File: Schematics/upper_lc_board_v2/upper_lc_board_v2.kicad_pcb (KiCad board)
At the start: 4 copper layers, 69.5 x 60 mm, 115 parts, among them J1 USB_C_Female_USB2_Small, J2 Stack Male Edge Connector, J3 SOL_CONN, J4 SOL_CONN, J5 HALL-1, J7 PT1, J8 PT1, Q2 AO3400A, Q3 AO3400A, Q4 2N7002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

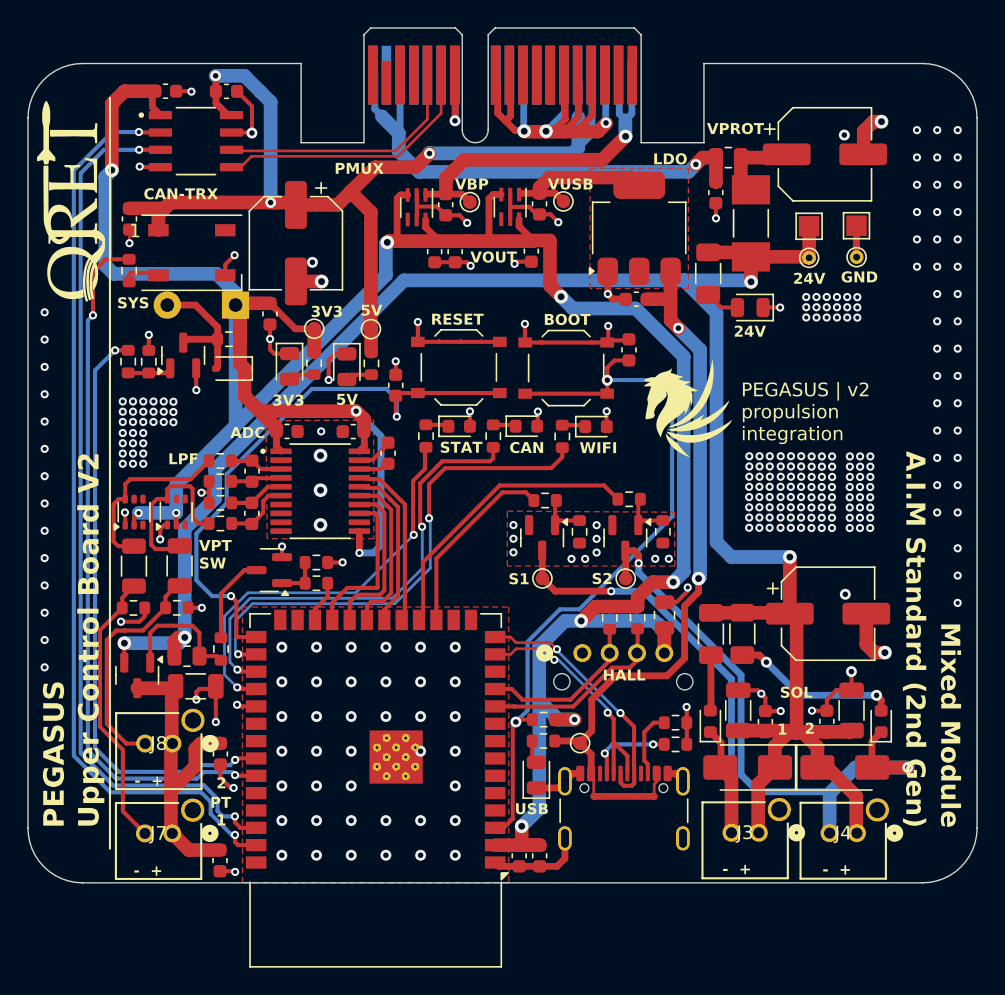
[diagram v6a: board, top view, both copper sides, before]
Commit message: tune diff pairs, increase track width on 5V rail
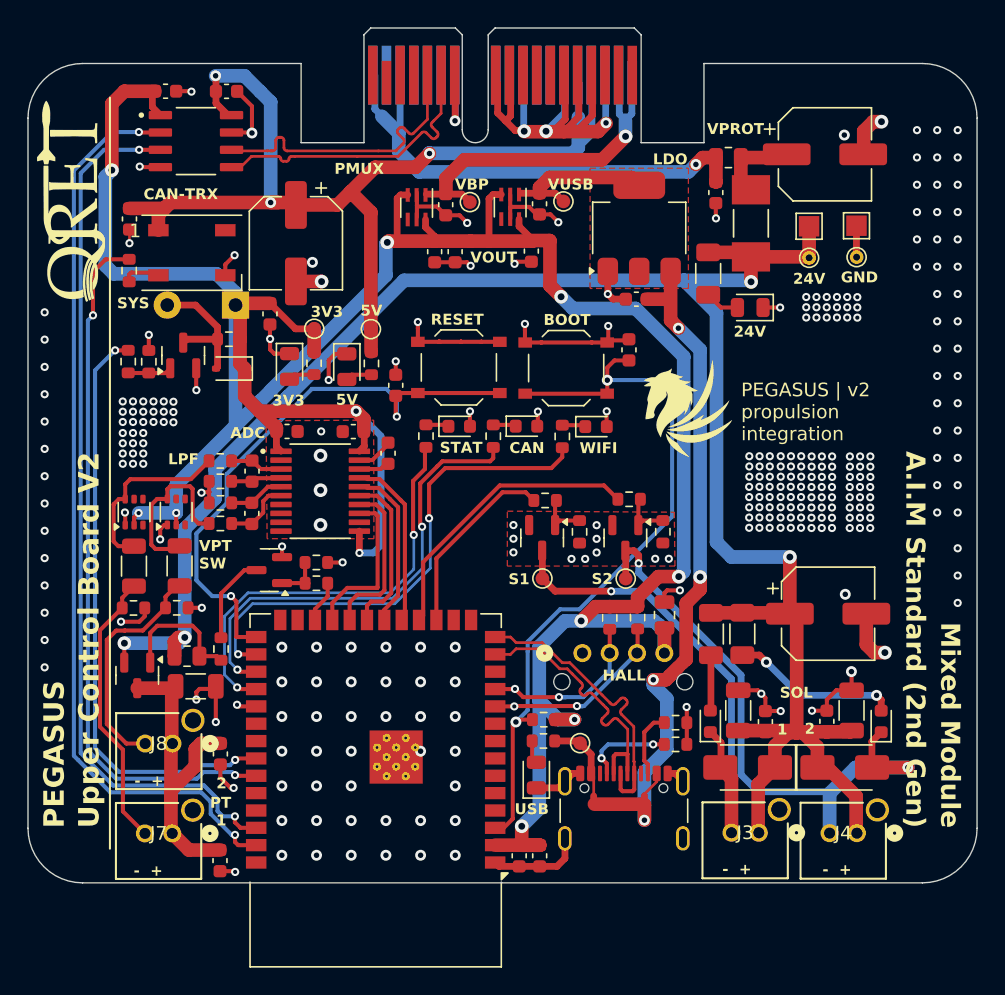
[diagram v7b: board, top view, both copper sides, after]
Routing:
- net 5V_USB: track 55.1 -> 60.3 mm, vias 2 -> 4
- net /ESP32-S3 Breakout Circuitry/USB_N: track 18.0 -> 21.4 mm, vias 2 -> 0
- net CAN_P: track 18.6 -> 21.7 mm
- net /ESP32-S3 Breakout Circuitry/USB_P: track 18.9 -> 21.7 mm, vias 2 -> 0
- net CAN_N: track 19.8 -> 21.7 mm
- net /ESP32-S3 Breakout Circuitry/GPIO_37: track 30.2 -> 31.7 mm
- net HALL_SCL: track 12.2 -> 13.0 mm, vias 0 -> 2
- net HALL_SDA: track 14.1 -> 14.2 mm, vias 0 -> 2

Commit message: refactor with new conns
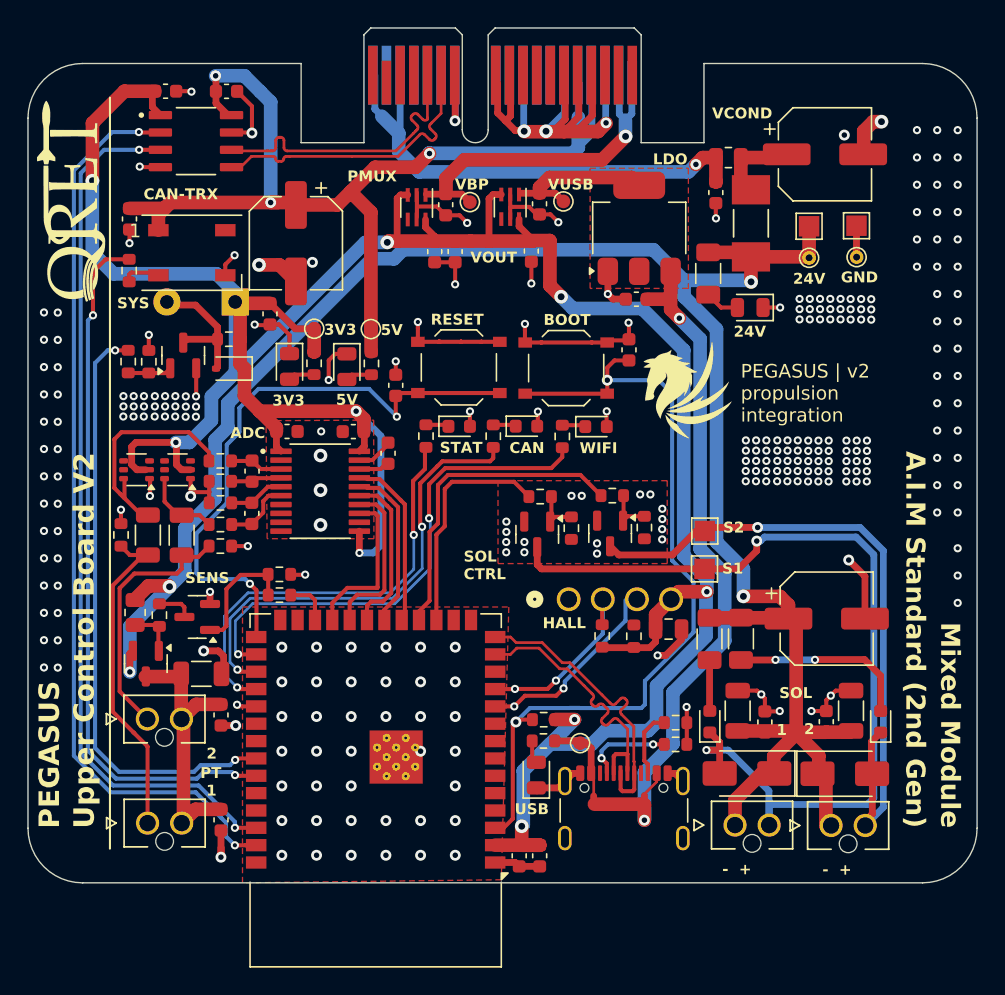
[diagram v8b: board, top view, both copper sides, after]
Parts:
- removed J8: PT1, ul_B02B-PASK-1:CONN_B02B-PASK-1_JST
- removed Q3: AO3400A, Package_TO_SOT_SMD:SOT-23
- removed R32, R35: 1k, Resistor_SMD:R_1206_3216Metric
- removed R34: 60, Resistor_SMD:R_0603_1608Metric
- removed R36: 200, Resistor_SMD:R_0603_1608Metric
- added J6: SOL_CONN, NANO-V-2-CONN:MOLEX_1053091102, F.Cu at (166.8, 115.8)
- added Q1: AO3400A, Package_TO_SOT_SMD:SOT-23, F.Cu at (145.3, 94.5)
- added R11: 60, Resistor_SMD:R_0603_1608Metric, F.Cu at (114.8, 94.5)
- added R12: 1k, Resistor_SMD:R_1206_3216Metric, F.Cu at (116.8, 94.5)
- added R14: 60, Resistor_SMD:R_0603_1608Metric, F.Cu at (122.1, 95.3)
- added R26: 200, Resistor_SMD:R_0603_1608Metric, F.Cu at (150.8, 91.6)
- D11, D12: value SS34 -> BAV199DW; footprint Diode_SMD:D_SMA -> Package_TO_SOT_SMD:SOT-363_SC-70-6
- D13, D14: value BAV199DW -> SS34; footprint Package_TO_SOT_SMD:SOT-363_SC-70-6 -> Diode_SMD:D_SMA
- J3, J4: value SOL_CONN -> PT1; footprint ul_B02B-PASK-1:CONN_B02B-PASK-1_JST -> NANO-V-2-CONN:MOLEX_1053091102
- J5: footprint S04B_PASK_2-P:CONN4_S04B-PASK_JST -> NANO-H-4-CONN:CONN_SD-105313-100_04_MOL
- J7: value PT1 -> SOL_CONN; footprint ul_B02B-PASK-1:CONN_B02B-PASK-1_JST -> NANO-V-2-CONN:MOLEX_1053091102
- R17: value 200 -> 1k; footprint Resistor_SMD:R_0603_1608Metric -> Resistor_SMD:R_1206_3216Metric
- R18: value 100k -> 200
- R31: value 60 -> 100k
- TP10, TP8: footprint TestPoint:TestPoint_Pad_D1.0mm -> TestPoint:TestPoint_Pad_1.5x1.5mm
- moved D12 53.5 mm to (118.9, 89.8), turned to 180 degrees
- moved J4 52.6 mm to (116.7, 108.0)
- moved D14 52.6 mm to (167.8, 112.0), turned to 0 degrees
- moved D11 49.8 mm to (115.9, 89.8)
- moved D13 48.8 mm to (160.6, 112.0), turned to 180 degrees
- moved J3 44.8 mm to (116.7, 115.6)
- moved J7 41.2 mm to (159.8, 115.8)
- moved R31 37.9 mm to (153.1, 94.0), turned to 90 degrees
- moved R17 26.7 mm to (119.2, 94.5), turned to 90 degrees
- moved R18 26.3 mm to (122.1, 93.8), turned to 180 degrees
- moved TP10 11.9 mm to (157.5, 97.0)
- moved TP8 6.76 mm to (157.6, 94.2)
- moved R20 6.71 mm to (147.8, 94.0)
- moved R19 6.52 mm to (145.5, 91.7)
- moved Q5 6.29 mm to (120.4, 100.5)
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- renumbered C32 to C28, C33 to C5, R33 to R13
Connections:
- D11 pad 1: +24V -> GND
- D11 pad 2: SOL1_RET -> +3V3
- D12 pad 1: +24V -> GND
- D12 pad 2: SOL2_RET -> +3V3
- D13 pad 1: GND -> +24V
- D13 pad 2: +3V3 -> SOL1_RET
- D14 pad 1: GND -> +24V
- D14 pad 2: +3V3 -> SOL2_RET
- J3 pad 1: +24V -> /Sensing Circuitry/PT1
- J3 pad 2: SOL1_RET -> VPT
- J4 pad 1: +24V -> /Sensing Circuitry/PT2
- J4 pad 2: SOL2_RET -> VPT
- J7 pad 1: VPT -> +24V
- J7 pad 2: /Sensing Circuitry/PT1 -> SOL1_RET
- Q2 pad 3: SOL1_RET -> SOL2_RET
- R13 pad 2: Net-(D13A-K3A4) -> Net-(D11A-K3A4)
- R17 pad 1: Net-(Q2-G) -> /Sensing Circuitry/PT2
- R17 pad 2: VALVE1_CTRL -> Net-(D12A-K3A4)
- R18 pad 1: GND -> /Sensing Circuitry/PT2_CLAMPED
- R18 pad 2: Net-(Q2-G) -> Net-(D12A-K3A4)
- R19 pad 2: VALVE2_CTRL -> VALVE1_CTRL
- R31 pad 2: /Sensing Circuitry/PT1 -> Net-(Q2-G)
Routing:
- net SOL1_RET: track 38.2 -> 68.4 mm, vias 1 -> 2
- net Net-(D11A-K3A4): track 0.00 -> 17.1 mm
- net Net-(D13A-K3A4): track 13.3 -> 0.00 mm
- net Net-(D14A-K3A4): track 12.5 -> 0.00 mm
- net Net-(U9-G): track 9.63 -> 3.62 mm
- net Net-(D12A-K3A4): track 0.00 -> 5.64 mm
- net Net-(Q5-G): track 3.45 -> 9.05 mm
- net /ESP32-S3 Breakout Circuitry/ESP32_EN: track 54.5 -> 59.7 mm
- net SOL2_RET: track 44.3 -> 49.5 mm, vias 2 -> 1
- net /Sensing Circuitry/PT1: track 20.5 -> 24.3 mm
- net Net-(Q5-D): track 6.54 -> 2.72 mm
- net VPT: track 23.7 -> 20.4 mm
- net VALVE1_CTRL: track 13.9 -> 16.7 mm
- net GND: track 170.0 -> 167.6 mm, vias 300 -> 280
- net /Sensing Circuitry/PT2: track 16.8 -> 18.9 mm
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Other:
- board text added: "PB-FREE"
- board text added: "SENS"
- board text added: "SOL CTRL"
- board text added: "VCOND"
- board text removed: "LPF"
- board text removed: "VPROT"
- board text removed: "VPT SW"
